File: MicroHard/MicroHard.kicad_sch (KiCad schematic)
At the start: 0 parts

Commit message: fpg
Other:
- added sheet FPGA (FPGA.kicad_sch)
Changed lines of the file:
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@@
 	)
 	(sheet
-		(at 116.84 76.2)
+		(at 82.804 16.002)
 		(size 40.64 45.72)
 		(fields_autoplaced yes)
@@
 		)
 		(property "Sheetname" "MCU"
-			(at 116.84 75.4884 0)
+			(at 82.804 15.2904 0)
 			(effects
 				(font
@@
 		)
 		(property "Sheetfile" "mcu.kicad_sch"
-			(at 116.84 122.5046 0)
+			(at 82.804 62.3066 0)
 			(effects
 				(font
@@
 				)
 			)
+		)
+	)
+	(sheet
+		(at 134.366 15.748)
+		(size 39.878 45.974)
+		(fields_autoplaced yes)
+		(stroke
+			(width 0.1524)
+			(type solid)
+		)
+		(fill
+			(color 0 0 0 0.0000)
+		)
+		(property "Sheetname" "FPGA"
+			(at 134.366 15.0364 0)
+			(effects
+				(font
+					(size 1.27 1.27)
+				)
+				(justify left bottom)
+			)
+		)
+		(property "Sheetfile" "FPGA.kicad_sch"
+			(at 134.366 62.3066 0)
+			(effects
+				(font
+					(size 1.27 1.27)
+				)
+				(justify left top)
+			)
+		)
+		(instances
+			(project "MicroHard"
+				(path "/578bd531-a491-4b15-a479-460d159ffc14"
+					(page "4")
+				)
+			)

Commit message: MCU schematic
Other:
- added sheet Display (display.kicad_sch)
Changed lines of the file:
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@@
+	)
+	(sheet
+		(at 88.9 88.9)
+		(size 60.96 55.88)
+		(fields_autoplaced yes)
+		(stroke
+			(width 0.1524)
+			(type solid)
+		)
+		(fill
+			(color 0 0 0 0.0000)
+		)
+		(property "Sheetname" "Display"
+			(at 88.9 88.1884 0)
+			(effects
+				(font
+					(size 1.27 1.27)
+				)
+				(justify left bottom)
+			)
+		)
+		(property "Sheetfile" "display.kicad_sch"
+			(at 88.9 145.3646 0)
+			(effects
+				(font
+					(size 1.27 1.27)
+				)
+				(justify left top)
+			)
+		)
+		(instances
+			(project "MicroHard"
+				(path "/578bd531-a491-4b15-a479-460d159ffc14"
+					(page "9")
+				)
+			)
+		)
 	)
 	(sheet

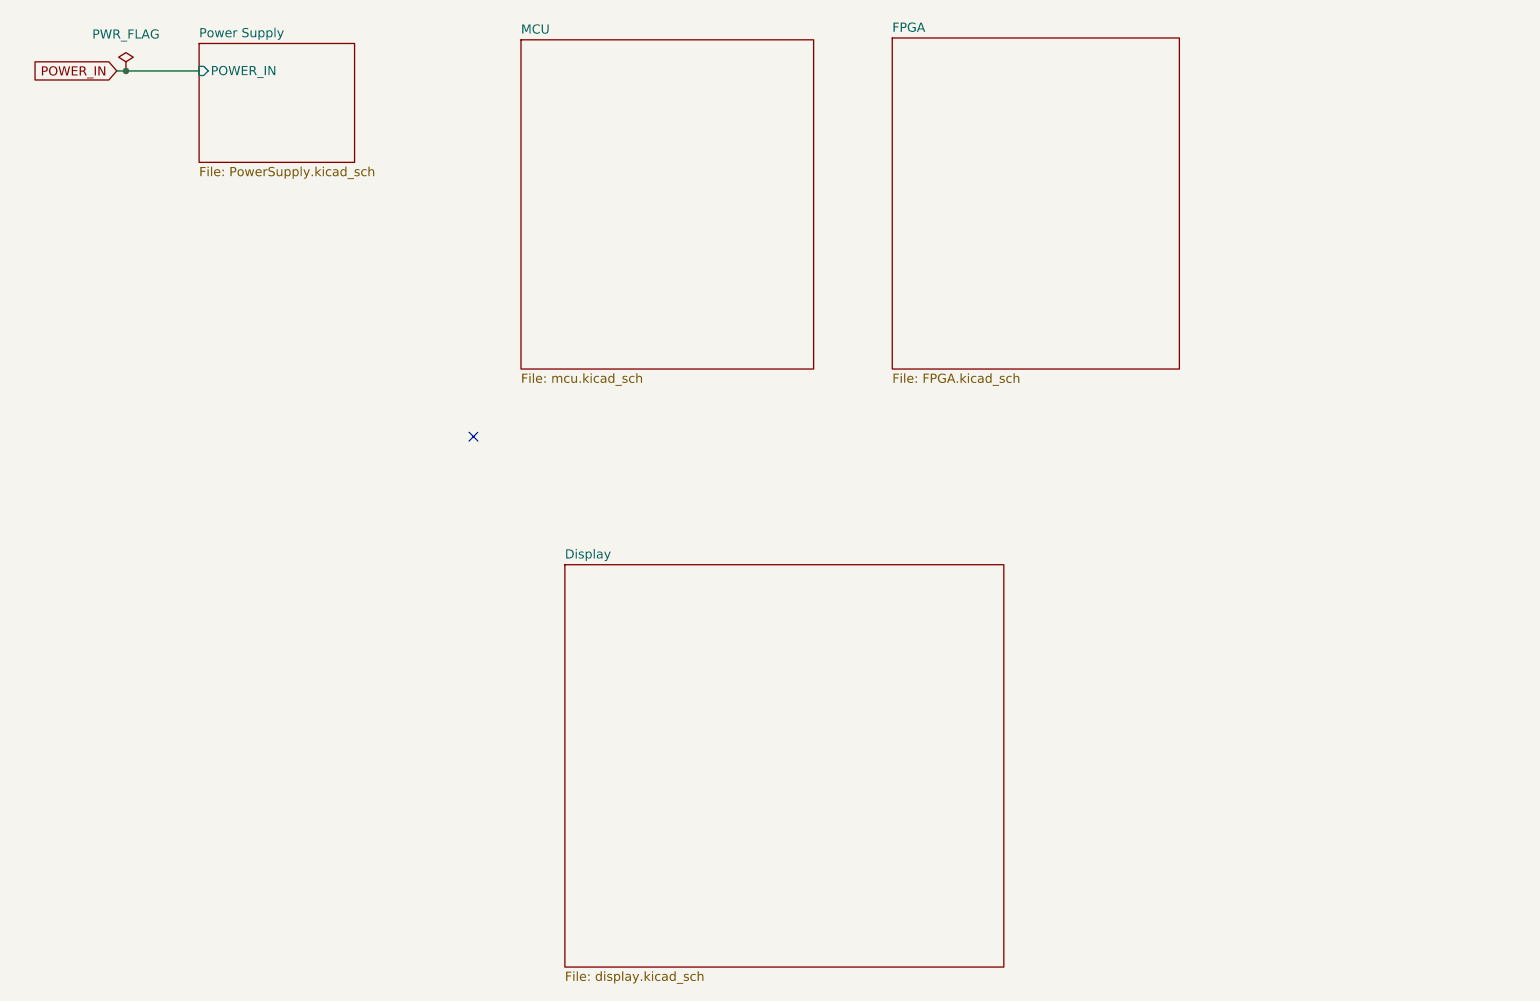
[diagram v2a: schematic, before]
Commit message: feat: VGA out lines from FPGA drawn
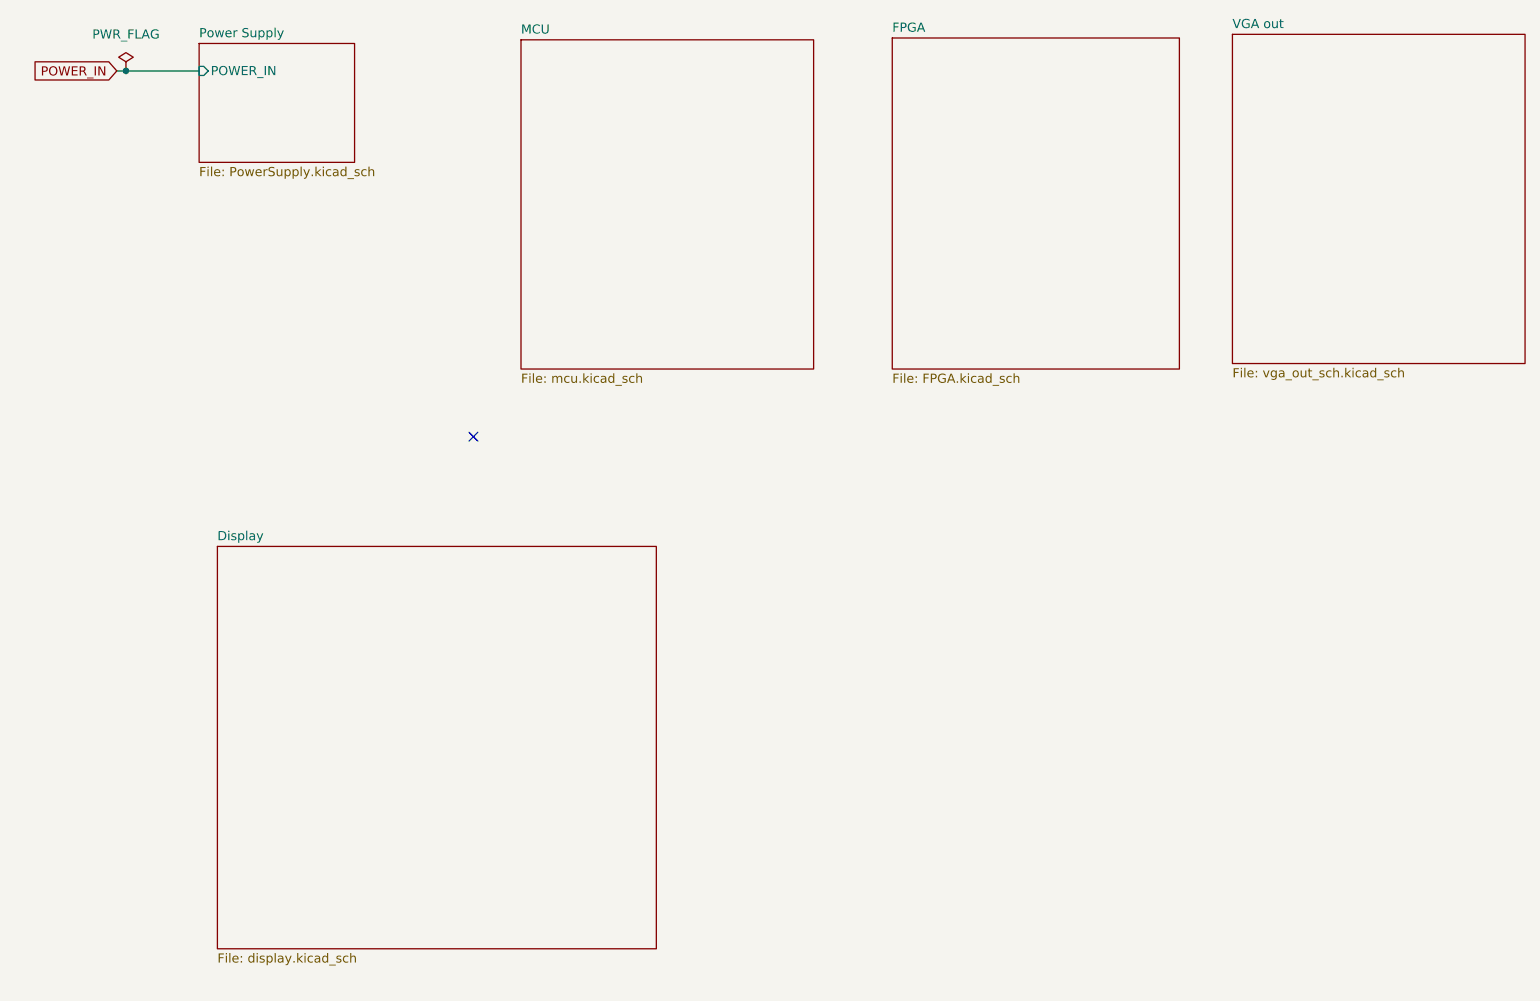
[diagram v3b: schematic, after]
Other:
- added sheet VGA out (vga_out_sch.kicad_sch)
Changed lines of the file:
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@@
 	)
 	(sheet
-		(at 88.9 88.9)
+		(at 40.64 86.36)
 		(size 60.96 55.88)
 		(fields_autoplaced yes)
@@
 		)
 		(property "Sheetname" "Display"
-			(at 88.9 88.1884 0)
+			(at 40.64 85.6484 0)
 			(effects
 				(font
@@
 		)
 		(property "Sheetfile" "display.kicad_sch"
-			(at 88.9 145.3646 0)
+			(at 40.64 142.8246 0)
 			(effects
 				(font
@@
 				)
 			)
+		)
+	)
+	(sheet
+		(at 181.61 15.24)
+		(size 40.64 45.72)
+		(fields_autoplaced yes)
+		(stroke
+			(width 0.1524)
+			(type solid)
+		)
+		(fill
+			(color 0 0 0 0.0000)
+		)
+		(property "Sheetname" "VGA out"
+			(at 181.61 14.5284 0)
+			(effects
+				(font
+					(size 1.27 1.27)
+				)
+				(justify left bottom)
+			)
+		)
+		(property "Sheetfile" "vga_out_sch.kicad_sch"
+			(at 181.61 61.5446 0)
+			(effects
+				(font
+					(size 1.27 1.27)
+				)
+				(justify left top)
+			)
+		)
+		(instances
+			(project "MicroHard"
+				(path "/578bd531-a491-4b15-a479-460d159ffc14"
+					(page "10")
+				)
+			)

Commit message: Finish display
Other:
- sheet Power Supply ports: added none; removed POWER_IN
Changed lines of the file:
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@@
 		(company "MicroHard")
 	)
-	(junction
-		(at 27.94 20.32)
-		(diameter 0)
-		(color 0 0 0 0)
-	)
 	(no_connect
 		(at 76.2 71.12)
 	)
-	(wire
-		(pts
-			(xy 27.94 20.32) (xy 38.1 20.32)
-		)
-		(stroke
-			(width 0)
-			(type default)
-		)
-	)
-	(wire
-		(pts
-			(xy 26.67 20.32) (xy 27.94 20.32)
-		)
-		(stroke
-			(width 0)
-			(type default)
-		)
-	)
 	(image
 		(at 269.24 173.99)
@@
 		)
 	)
-	(global_label "POWER_IN"
-		(shape input)
-		(at 26.67 20.32 180)
-		(fields_autoplaced yes)
-		(effects
-			(font
-				(size 1.27 1.27)
-			)
-			(justify right)
-		)
-		(property "Intersheetrefs" "${INTERSHEET_REFS}"
-			(at 14.311 20.32 0)
-			(effects
-				(font
-					(size 1.27 1.27)
-				)
-				(justify right)
-				(hide yes)
-			)
-		)
-	)
-	(symbol
-		(lib_id "power:PWR_FLAG")
-		(at 27.94 20.32 0)
-		(unit 1)
-		(exclude_from_sim no)
-		(in_bom yes)
-		(on_board yes)
-		(dnp no)
-		(fields_autoplaced yes)
-		(property "Reference" "#FLG01"
-			(at 27.94 18.415 0)
-			(effects
-				(font
-					(size 1.27 1.27)
-				)
-				(hide yes)
-			)
-		)
-		(property "Value" "PWR_FLAG"
-			(at 27.94 15.24 0)
-			(effects
-				(font
-					(size 1.27 1.27)
-				)
-			)
-		)
-		(property "Footprint" ""
-			(at 27.94 20.32 0)
-			(effects
-				(font
-					(size 1.27 1.27)
-				)
-				(hide yes)
-			)
-		)
-		(property "Datasheet" "~"
-			(at 27.94 20.32 0)
-			(effects
-				(font
-					(size 1.27 1.27)
-				)
-				(hide yes)
-			)
-		)
-		(property "Description" "Special symbol for telling ERC where power comes from"
-			(at 27.94 20.32 0)
-			(effects
-				(font
-					(size 1.27 1.27)
-				)
-				(hide yes)
-			)
-		)
-		(pin "1"
-		)
-		(instances
-			(project ""
-				(path "/578bd531-a491-4b15-a479-460d159ffc14"
-					(reference "#FLG01")
-					(unit 1)
-				)
-			)
-		)
-	)
 	(sheet
 		(at 82.804 16.002)
@@
 	)
 	(sheet
-		(at 38.1 16.51)
+		(at 49.53 24.13)
 		(size 21.59 16.51)
 		(fields_autoplaced yes)
@@
 		)
 		(property "Sheetname" "Power Supply"
-			(at 38.1 15.7984 0)
+			(at 49.53 23.4184 0)
 			(effects
 				(font
@@
 		)
 		(property "Sheetfile" "PowerSupply.kicad_sch"
-			(at 38.1 33.6046 0)
+			(at 49.53 41.2246 0)
 			(effects
 				(font
@@
 			)
 		)
-		(pin "POWER_IN" input
-			(at 38.1 20.32 180)
-			(effects
-				(font
-					(size 1.27 1.27)
-				)
-				(justify left)
-			)
-		)

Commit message: footprints
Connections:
- no-connect marks 1 -> 0
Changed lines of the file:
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@@
 		(company "MicroHard")
-	)
-	(no_connect
-		(at 76.2 71.12)
 	)
 	(image
